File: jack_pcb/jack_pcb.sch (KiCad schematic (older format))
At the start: 48 parts

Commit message: jack pcb work
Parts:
- removed J? (x47): PJ301M-12, symbol eurocad:PJ301M-12
- added J10, J11, J12, J13, J14, J15, J16, J17, J18, J19, J2, J20, J21, J22, J23, J24, J25, J26, J27, J28, J29, J3, J30, J31, J32, J4, J5, J6, J7, J8, J9: PJ301M-12, symbol eurocad:PJ301M-12
- added J33, J34, J35, J36, J37, J38, J39, J40, J41, J42, J43, J44, J45, J46, J47, J48: AudioJack3, symbol Connector:AudioJack3
- added J?: Conn_02x18_Top_Bottom, symbol Connector_Generic:Conn_02x18_Top_Bottom
- added J?: Conn_02x10_Top_Bottom, symbol Connector_Generic:Conn_02x10_Top_Bottom
- gave numbers to parts that had none: 1
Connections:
- net labels added: 1, 10, 11, 12, 13, 14, 15, 16, 17, 18, 19, 2, 20, 21, 22, 23, 24, 25, 26, 27, 28, 29, 3, 30, 31, 32, 4, 5, 6, 7, 8, 9, GND, IN1, IN10, IN11, IN12, IN13, IN14, IN15, IN16, IN2, IN3, IN4, IN5, IN6, IN7, IN8, IN9, VCC
- wire segments 0 -> 137

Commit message: jack pcb update
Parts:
- removed J33, J34, J35, J36, J37, J38, J39, J40, J41, J42, J43, J44, J45, J46, J47, J48: AudioJack3, symbol Connector:AudioJack3
- added C?: .1uF, symbol Device:C_Small
- added D?: 1N914, Diode_THT:D_DO-35_SOD27_P7.62mm_Horizontal, symbol Diode:1N914
- added J? (x6): RJ45, symbol Connector:RJ45
- added J? (x3): DIN-5, symbol Connector:DIN-5
- added R? (x2): 280, symbol Device:R_Small_US
- added U?: 6N138, symbol Isolator:6N138
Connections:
- net labels added: +12V, +3V3, +5V, MIDI_IN, MIDI_NEG, MIDI_POS
- net labels removed: VCC
- wire segments 137 -> 138
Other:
- note added: "1/8" output jacks to synth modules"
- note added: "MIDI Input"
- note added: "rj45 inputs from user interface"
- note added: "visual output system"
- moved on the sheet: J?

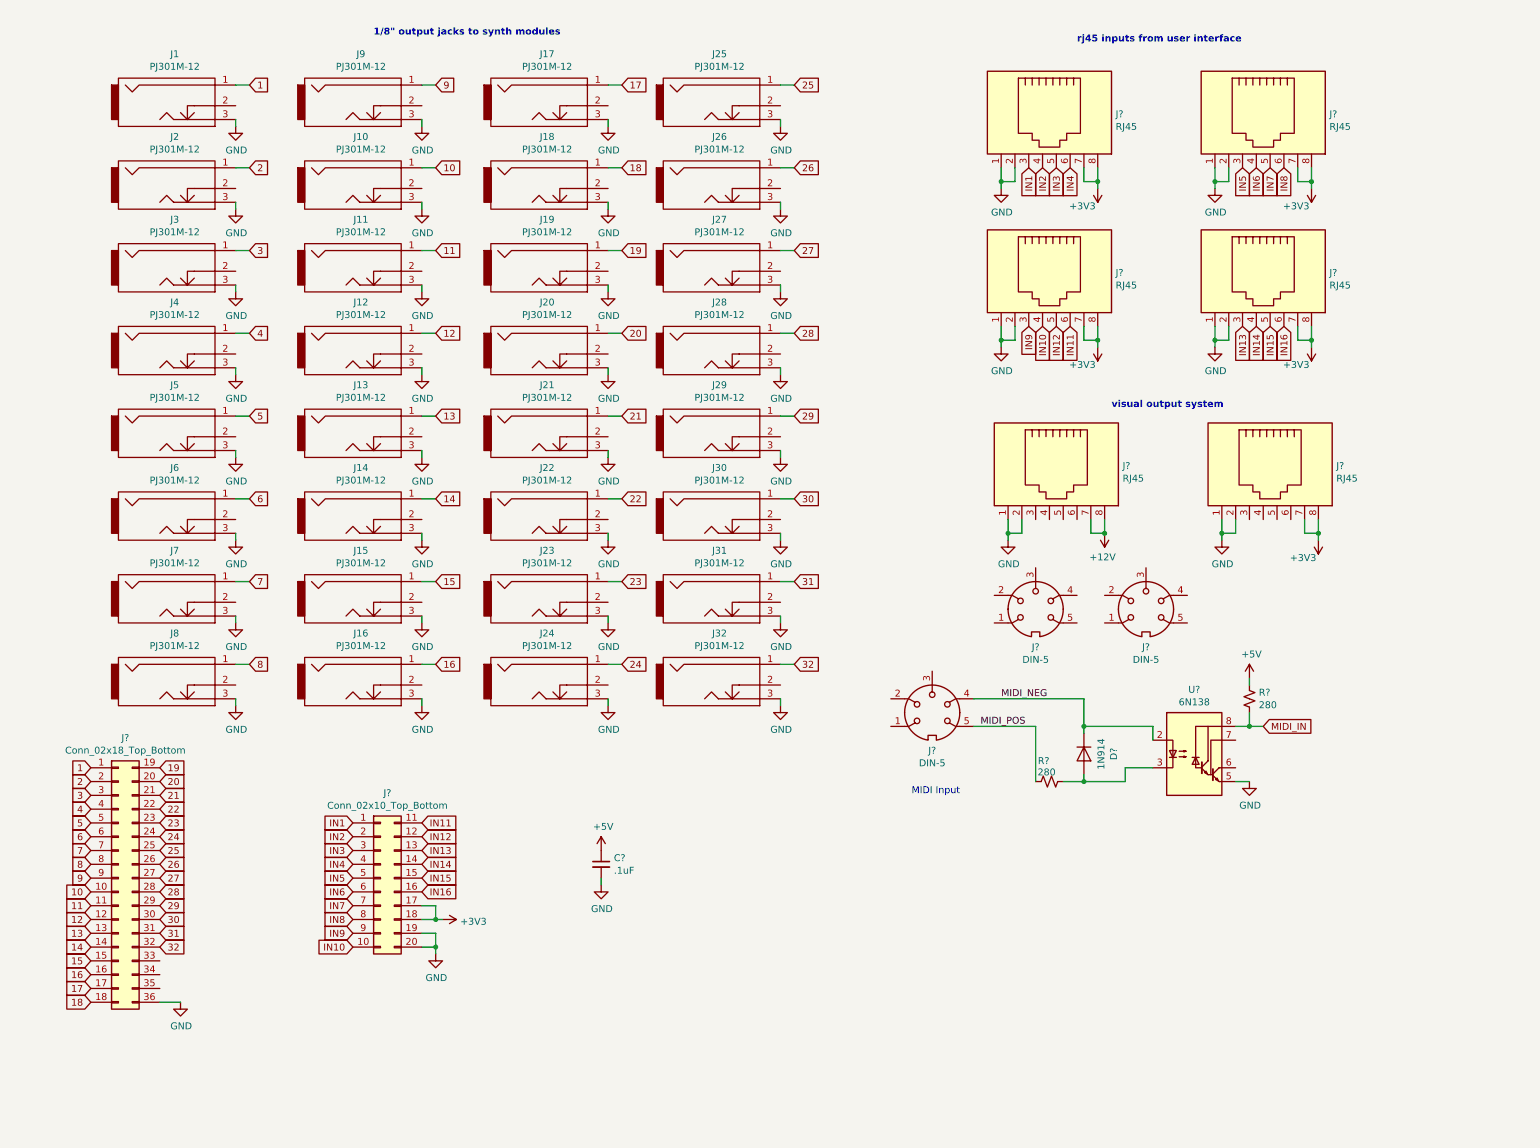
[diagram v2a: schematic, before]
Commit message: jack board updates
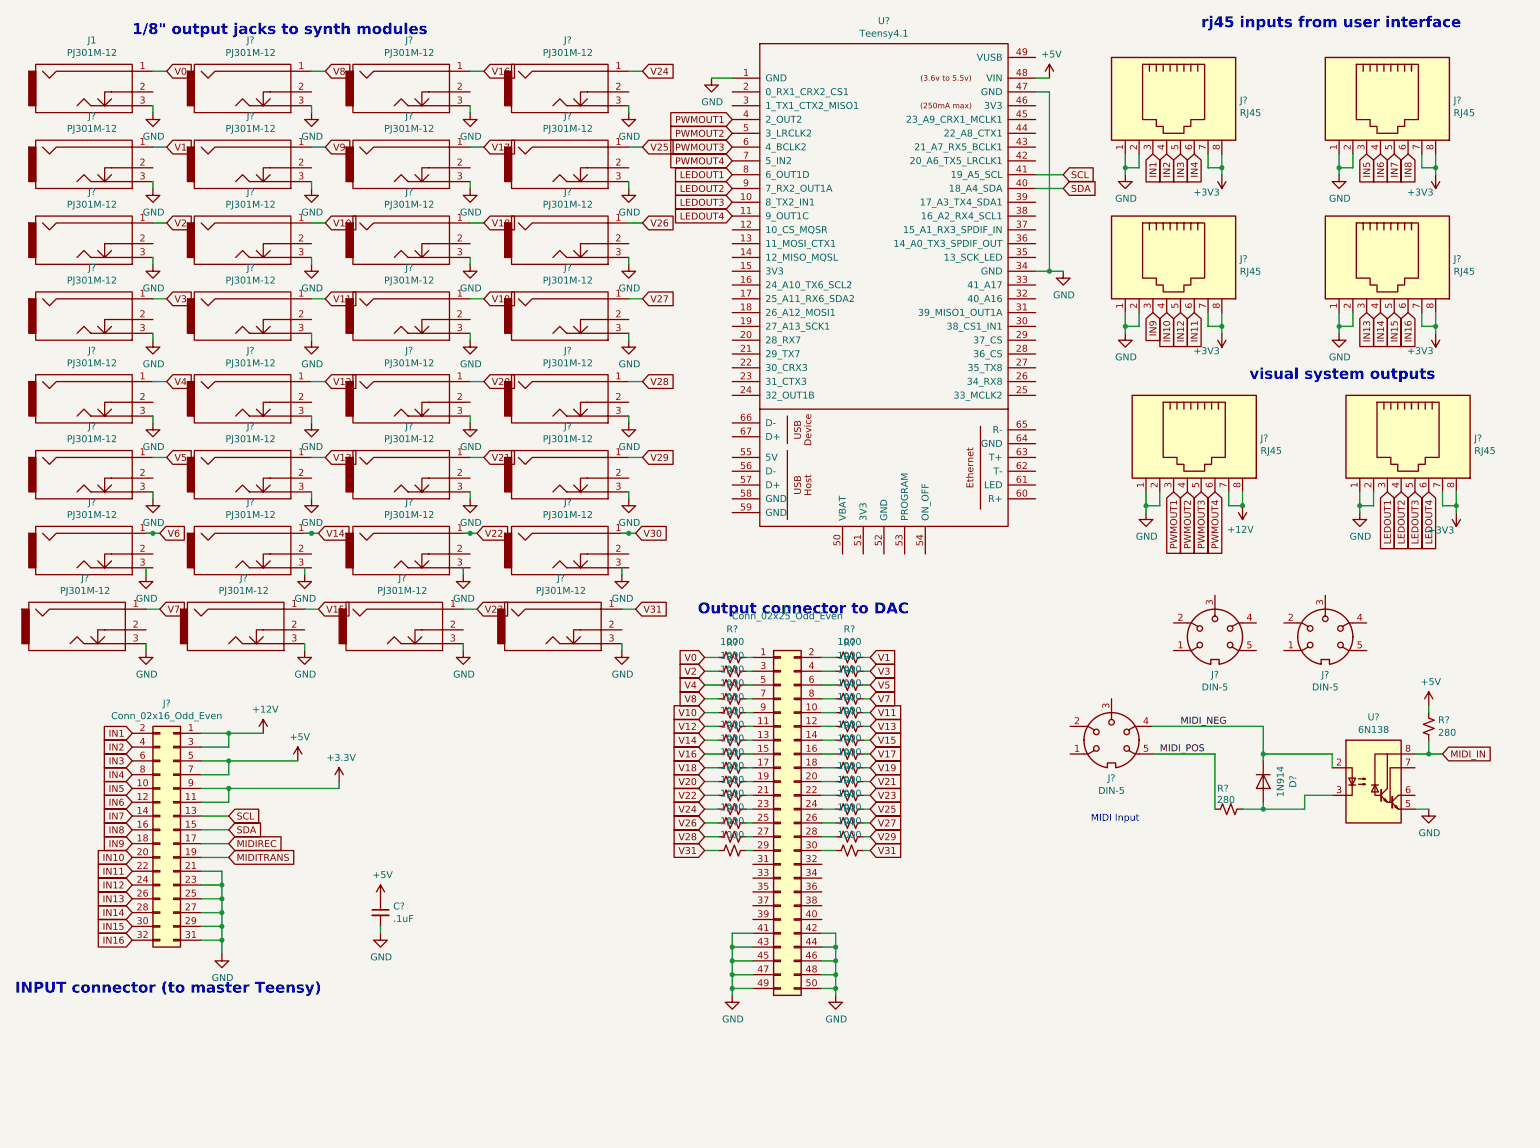
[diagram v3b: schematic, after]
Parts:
- removed J10, J11, J12, J13, J14, J15, J16, J17, J18, J19, J2, J20, J21, J22, J23, J24, J25, J26, J27, J28, J29, J3, J30, J31, J32, J4, J5, J6, J7, J8, J9: PJ301M-12, symbol eurocad:PJ301M-12
- removed J?: Conn_02x18_Top_Bottom, symbol Connector_Generic:Conn_02x18_Top_Bottom
- removed J?: Conn_02x10_Top_Bottom, symbol Connector_Generic:Conn_02x10_Top_Bottom
- added J?: Conn_02x16_Odd_Even, symbol Connector_Generic:Conn_02x16_Odd_Even
- added J?: Conn_02x25_Odd_Even, symbol Connector_Generic:Conn_02x25_Odd_Even
- added J? (x31): PJ301M-12, symbol eurocad:PJ301M-12
- added R? (x30): 1000, symbol Device:R_Small_US
- added U?: Teensy4.1, symbol teensy:Teensy4.1
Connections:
- net +12V: now also J?.1 (Pin_1), J?.3 (Pin_3)
- net +3V3: now also J?.11 (Pin_11), J?.9 (Pin_9)
- net +5V: now also J?.5 (Pin_5), J?.7 (Pin_7), U?.48 (VIN)
- net GND: now also J?.21 (Pin_21), J?.23 (Pin_23), J?.25 (Pin_25), J?.27 (Pin_27), J?.29 (Pin_29), J?.3, J?.3, J?.3, J?.3, J?.3, J?.3, J?.3, J?.3, J?.3, J?.3, J?.3, J?.3, J?.3, J?.3, J?.3, J?.3, J?.3, J?.3, J?.3, J?.3, J?.3, J?.3, J?.3, J?.3, J?.3, J?.3, J?.3, J?.31 (Pin_31), J?.41 (Pin_41), J?.42 (Pin_42), J?.43 (Pin_43), J?.44 (Pin_44), J?.45 (Pin_45), J?.46 (Pin_46), J?.47 (Pin_47), J?.48 (Pin_48), J?.49 (Pin_49), J?.50 (Pin_50), U?.1 (GND), U?.34 (GND), U?.47 (GND)
- net IN1: now also J?.2 (Pin_2)
- net IN10: now also J?.20 (Pin_20)
- net IN11: now also J?.22 (Pin_22)
- net IN12: now also J?.24 (Pin_24)
- net IN13: now also J?.26 (Pin_26)
- net IN14: now also J?.28 (Pin_28)
- net IN15: now also J?.30 (Pin_30)
- net IN16: now also J?.32 (Pin_32)
- net IN2: now also J?.4 (Pin_4)
- net IN3: now also J?.6 (Pin_6)
- net IN4: now also J?.8 (Pin_8)
- net IN5: now also J?.10 (Pin_10)
- net IN6: now also J?.12 (Pin_12)
- net IN7: now also J?.14 (Pin_14)
- net IN8: now also J?.16 (Pin_16)
- net IN9: now also J?.18 (Pin_18)
- net PWMOUT1: now reaches J?.3
- net PWMOUT1: now also U?.4 (2_OUT2)
- net PWMOUT2: now reaches J?.4
- net PWMOUT2: now also U?.5 (3_LRCLK2)
- net PWMOUT3: now reaches J?.5
- net PWMOUT3: now also U?.6 (4_BCLK2)
- net PWMOUT4: now reaches J?.6
- net PWMOUT4: now also U?.7 (5_IN2)
- net LEDOUT1: now reaches J?.3
- net LEDOUT1: now also U?.8 (6_OUT1D)
- net LEDOUT2: now reaches J?.4
- net LEDOUT2: now also U?.9 (7_RX2_OUT1A)
- net LEDOUT3: now reaches J?.5
- net LEDOUT3: now also U?.10 (8_TX2_IN1)
- net LEDOUT4: now reaches J?.6
- net LEDOUT4: now also U?.11 (9_OUT1C)
- net 1 renamed V0
- net V0: now also R?.2
- new net: J?.1 (Pin_1), R?.1
- new net: J?.10 (Pin_10), R?.2
- new net: J?.11 (Pin_11), R?.1
- new net: J?.12 (Pin_12), R?.2
- new net: J?.13 (Pin_13), R?.1
- new net: J?.14 (Pin_14), R?.2
- new net: J?.15 (Pin_15), R?.1
- new net: J?.16 (Pin_16), R?.2
- new net: J?.17 (Pin_17), R?.1
- new net: J?.18 (Pin_18), R?.2
- new net: J?.19 (Pin_19), R?.1
- new net: J?.2 (Pin_2), R?.2
- new net: J?.20 (Pin_20), R?.2
- new net: J?.21 (Pin_21), R?.1
- new net: J?.22 (Pin_22), R?.2
- new net: J?.23 (Pin_23), R?.1
- new net: J?.24 (Pin_24), R?.2
- new net: J?.25 (Pin_25), R?.1
- new net: J?.26 (Pin_26), R?.2
- new net: J?.27 (Pin_27), R?.1
- new net: J?.28 (Pin_28), R?.2
- new net: J?.29 (Pin_29), R?.1
- new net: J?.3 (Pin_3), R?.1
- new net: J?.30 (Pin_30), R?.2
- new net: J?.4 (Pin_4), R?.2
- new net: J?.5 (Pin_5), R?.1
- new net: J?.6 (Pin_6), R?.2
- new net: J?.7 (Pin_7), R?.1
- new net: J?.8 (Pin_8), R?.2
- new net: J?.9 (Pin_9), R?.1
- new net MIDIREC: J?.17 (Pin_17)
- new net MIDITRANS: J?.19 (Pin_19)
- new net SCL: J?.13 (Pin_13), U?.41 (19_A5_SCL)
- new net SDA: J?.15 (Pin_15), U?.40 (18_A4_SDA)
- new net V1: J?.1, R?.1
- new net V10: J?.1, R?.2
- new net V11: J?.1, R?.1
- new net V12: J?.1, R?.2
- new net V13: J?.1, R?.1
- new net V14: J?.1, R?.2
- new net V15: J?.1, R?.1
- new net V16: J?.1, R?.2
- new net V17: J?.1, R?.1
- new net V18: J?.1, R?.2
- new net V19: J?.1, R?.1
- new net V2: J?.1, R?.2
- new net V20: J?.1, R?.2
- new net V21: J?.1, R?.1
- new net V22: J?.1, R?.2
- new net V23: J?.1, R?.1
- new net V24: J?.1, R?.2
- new net V25: J?.1, R?.1
- new net V26: J?.1, R?.2
- new net V27: J?.1, R?.1
- new net V28: J?.1, R?.2
- new net V29: J?.1, R?.1
- new net V3: J?.1, R?.1
- new net V30: J?.1
- new net V31: J?.1, R?.1, R?.2
- new net V4: J?.1, R?.2
- new net V5: J?.1, R?.1
- new net V6: J?.1
- new net V7: J?.1, R?.1
- new net V8: J?.1, R?.2
- new net V9: J?.1
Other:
- note added: "INPUT connector (to master Teensy)"
- note added: "Output connector to DAC"
- note added: "visual system outputs"
- note removed: "visual output system"
- moved on the sheet: C?, D?, J1, J?, R?, U?

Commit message: jack board updates
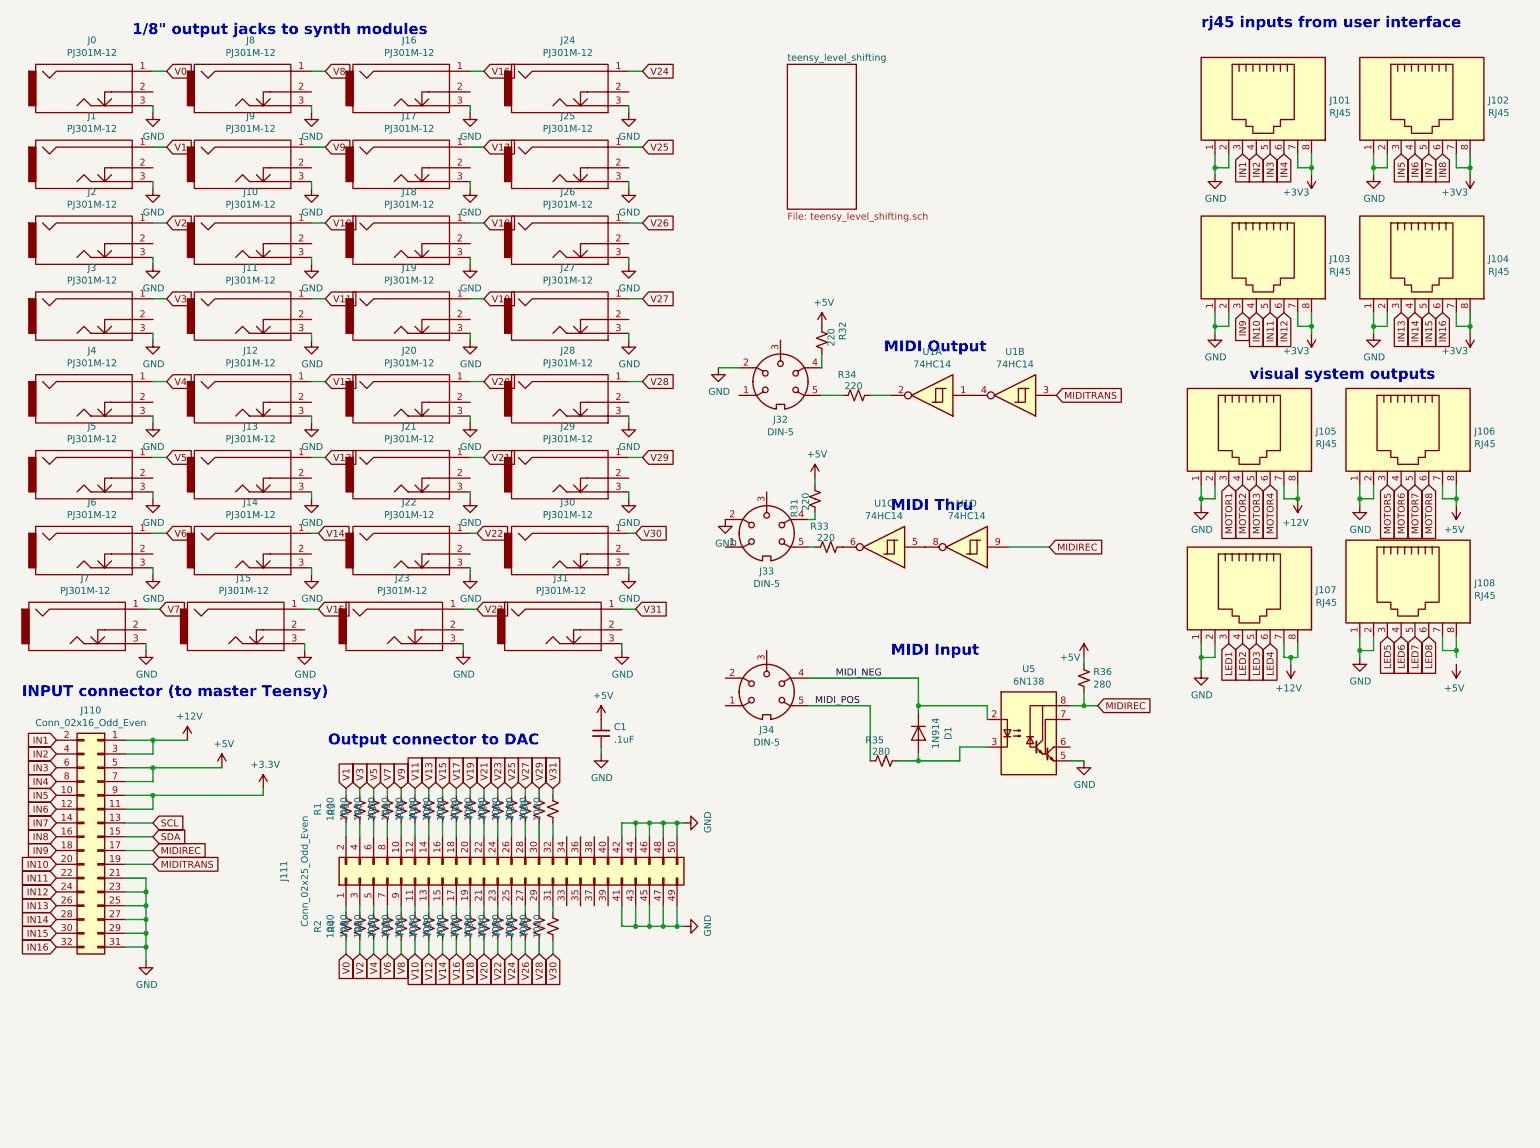
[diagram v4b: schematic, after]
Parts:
- removed U?: Teensy4.1, symbol teensy:Teensy4.1
- added J107, J108: RJ45, Connector_RJ:RJ45_Amphenol_54602-x08_Horizontal, symbol Connector:RJ45
- added R31, R32, R33, R34: 220, Resistor_THT:R_Axial_DIN0207_L6.3mm_D2.5mm_P10.16mm_Horizontal, symbol Device:R_Small_US
- added R37, R38: 1000, Resistor_THT:R_Axial_DIN0207_L6.3mm_D2.5mm_P10.16mm_Horizontal, symbol Device:R_Small_US
- added U1: 74HC14, Package_DIP:DIP-14_W7.62mm_Socket_LongPads, symbol 74xx:74HC14
- C1: renamed from C?; footprint (none) -> Capacitor_THT:C_Axial_L3.8mm_D2.6mm_P7.50mm_Horizontal
- J0: renamed from J1; footprint (none) -> Eurocad:PJ301M-12
- J1, J10, J11, J12, J13, J14, J15, J16, J17, J18, J19, J2, J20, J21, J22, J23, J24, J25, J26, J27, J28, J29, J3, J30, J31, J4, J5, J6, J7, J8, J9: renamed from J?; footprint (none) -> Eurocad:PJ301M-12
- J101, J102, J103, J104, J105, J106: renamed from J?; footprint (none) -> Connector_RJ:RJ45_Amphenol_54602-x08_Horizontal
- J110: renamed from J?; footprint (none) -> Connector_PinSocket_2.54mm:PinSocket_2x16_P2.54mm_Vertical
- J111: renamed from J?; footprint (none) -> Connector_PinSocket_2.54mm:PinSocket_2x25_P2.54mm_Vertical
- J32, J33, J34: renamed from J?; footprint (none) -> Connector_PinSocket_2.54mm:PinSocket_1x05_P2.54mm_Vertical
- R1, R10, R11, R12, R13, R14, R15, R16, R17, R18, R19, R2, R20, R21, R22, R23, R24, R25, R26, R27, R28, R29, R3, R30, R35, R36, R4, R5, R6, R7, R8, R9: renamed from R?; footprint (none) -> Resistor_THT:R_Axial_DIN0207_L6.3mm_D2.5mm_P10.16mm_Horizontal
- U5: renamed from U?; footprint (none) -> Package_DIP:DIP-8_W7.62mm_Socket
- gave numbers to parts that had none: 1
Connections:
- net MIDI_IN is gone; now on net MIDIREC: R36.2, U5.8 (VCC)
- net +12V: now also J107.7, J107.8
- net +3V3: no longer J106.7, J106.8
- net +5V: now also J106.7, J106.8, R31.2, R32.1
- net GND: now also J14.3, J22.3, J30.3, J32.2, J33.2, J6.3, J107.1, J107.2, J108.1, J108.2
- net IN11: now also J103.5; no longer J103.6
- net IN12: now also J103.6; no longer J103.5
- net MIDIREC: now also U1.9
- net MIDITRANS: now also U1.3
- net V10: now also R12.2; no longer R10.2
- net V12: now also R14.2; no longer R12.2
- net V14: now also R16.2; no longer R14.2
- net V16: now also R18.2; no longer R16.2
- net V18: now also R20.2; no longer R18.2
- net V20: now also R22.2; no longer R20.2
- net V22: now also R24.2; no longer R22.2
- net V24: now also R26.2; no longer R24.2
- net V26: now also R28.2; no longer R26.2
- net V28: now also R30.2; no longer R28.2
- net V30: now also R38.2
- net V31: no longer R30.2
- net V6: now also R8.2
- net V8: now also R10.2; no longer R8.2
- net V9: now also R37.1
- net at J32.4: now also R32.2
- net at J32.5: now also R34.1
- net at J33.4: now also R31.1
- net at J33.5: now also R33.1
- net at J111.10 (Pin_10): now also R37.2; no longer R9.2
- net at J111.12 (Pin_12): now also R9.2; no longer R11.2
- net at J111.14 (Pin_14): now also R11.2; no longer R13.2
- net at J111.16 (Pin_16): now also R13.2; no longer R15.2
- net at J111.18 (Pin_18): now also R15.2; no longer R17.2
- net at J111.20 (Pin_20): now also R17.2; no longer R19.2
- net at J111.22 (Pin_22): now also R19.2; no longer R21.2
- net at J111.24 (Pin_24): now also R21.2; no longer R23.2
- net at J111.26 (Pin_26): now also R23.2; no longer R25.2
- net at J111.28 (Pin_28): now also R25.2; no longer R27.2
- net at J111.30 (Pin_30): now also R27.2; no longer R29.2
- net at J111.31 (Pin_31): now also R38.1
- net at J111.32 (Pin_32): now also R29.2
- net LEDOUT1 renamed MOTOR5
- net LEDOUT2 renamed MOTOR6
- net LEDOUT3 renamed MOTOR7
- net LEDOUT4 renamed MOTOR8
- net PWMOUT1 renamed MOTOR1
- net PWMOUT2 renamed MOTOR2
- net PWMOUT3 renamed MOTOR3
- net PWMOUT4 renamed MOTOR4
- new net: J108.7, J108.8
- new net: U1.1, U1.4
- new net: U1.5, U1.8
- new net: R33.2, U1.6
- new net: R34.2, U1.2
- new net LED1: J107.3
- new net LED2: J107.4
- new net LED3: J107.5
- new net LED4: J107.6
- new net LED5: J108.3
- new net LED6: J108.4
- new net LED7: J108.5
- new net LED8: J108.6
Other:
- note added: "MIDI Output"
- note added: "MIDI Thru"
- moved on the sheet: C1, D1, J101, J102, J103, J104, J105, J106, J110, J111, J32, J33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

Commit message: jack board modifications
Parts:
- added C? (x2): .1uF, Capacitor_THT:C_Axial_L3.8mm_D2.6mm_P7.50mm_Horizontal, symbol Device:C_Small
- C1: value .1uF -> 10uF Tantalum
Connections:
- net +5V: now also C?.1
- net GND: now also C?.1, C?.2
- net at J111.2 (Pin_2), R1.2: now also C?.2
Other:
- moved on the sheet: C1, J111, R1, R10, R11, R12, R13, R14, R15, R16, R17, R18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
